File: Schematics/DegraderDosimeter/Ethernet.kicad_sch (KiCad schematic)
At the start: 38 parts, among them J1 KRJ-CB4.2GYZNL, U1 LAN8742A, U2 USBLC6-4SC6, U3 H1102NL, Y1 25.000MHz

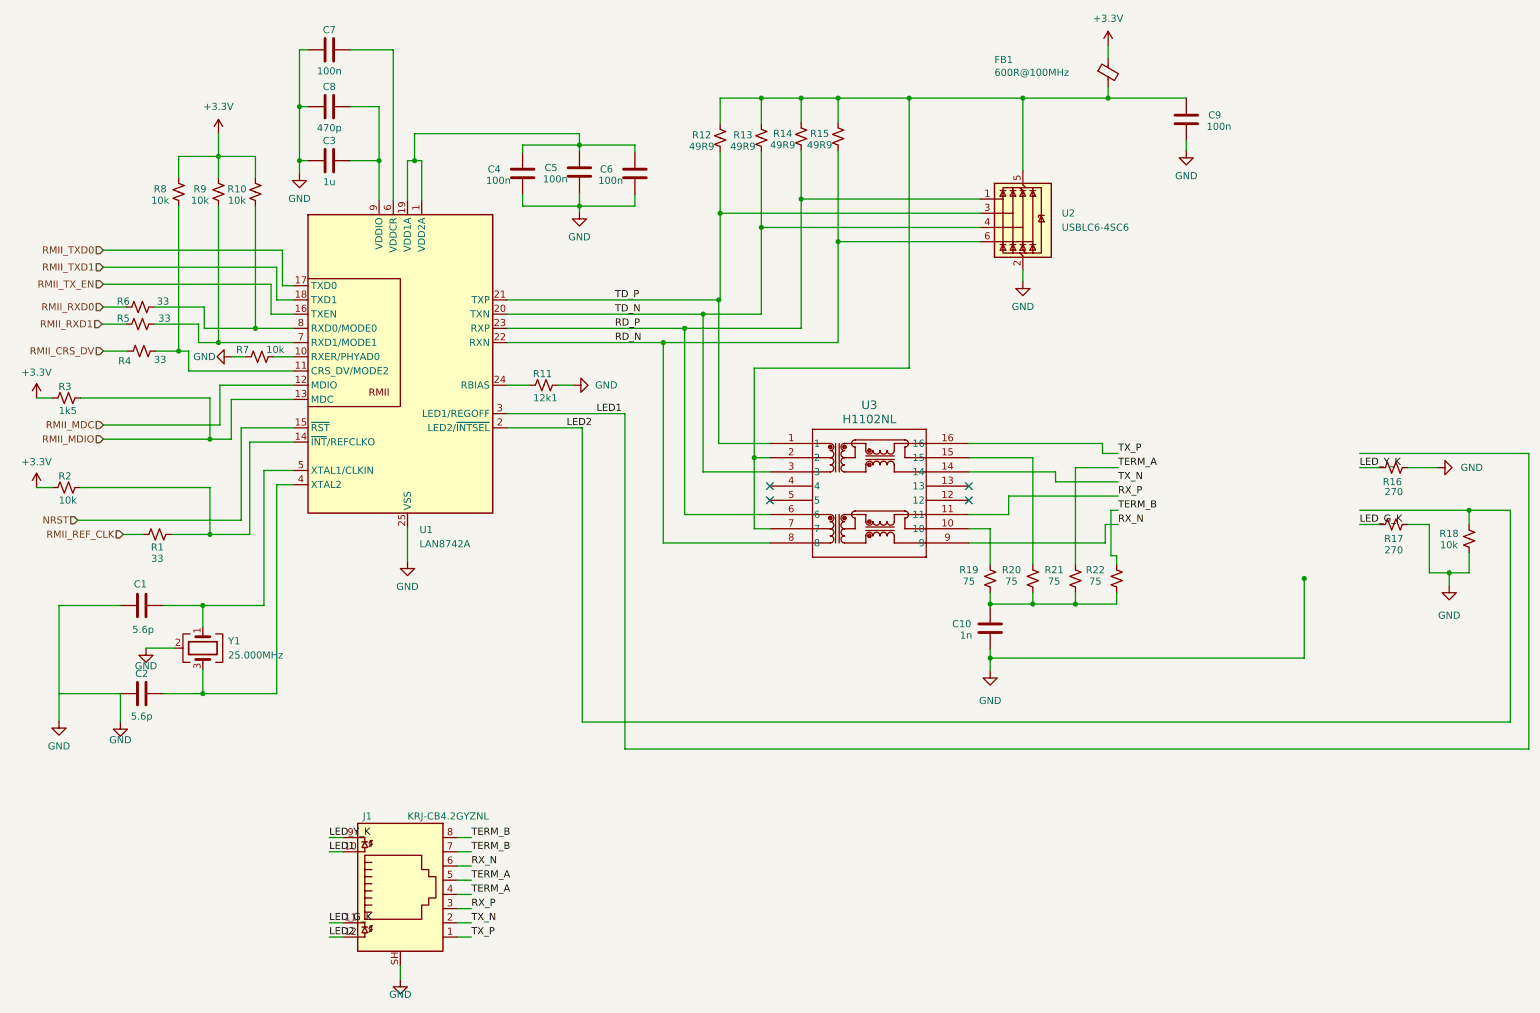
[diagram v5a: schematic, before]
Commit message: Use 1206 for every resistor in the project
The Ethernet sheet was the only one on 0402, set that way to match the
MB1364 BOM. The other four sheets already used
Resistor_SMD:R_1206_3216Metric_Pad1.30x1.75mm_HandSolder, so move the
20 Ethernet resistors to the same footprint. All 37 resistors in the
project now share one package, which suits hand assembly.

This deviates from the ST reference for the eight resistors on the
high-speed nets: R3-R6 (33R RMII series) and R12-R15 (49R9 centre-tap
terminations). 1206 has more parasitic inductance and larger pads than
the 0402 parts ST fits. 100BASE-TX is tolerant enough that this should
still work, but 0402 would be the better choice on those eight.

This commit also captures schematic edits made in KiCad outside this
session: a project-wide re-annotation and the removal of R21/R22, the
two 75R resistors that terminated the jack's unused pairs.

Co-Authored-By: Claude Opus 5 <noreply@anthropic.com>
Claude-Session: https://claude.ai/code/session_01Ej9hevrS5JU2uwVi6UHQUS
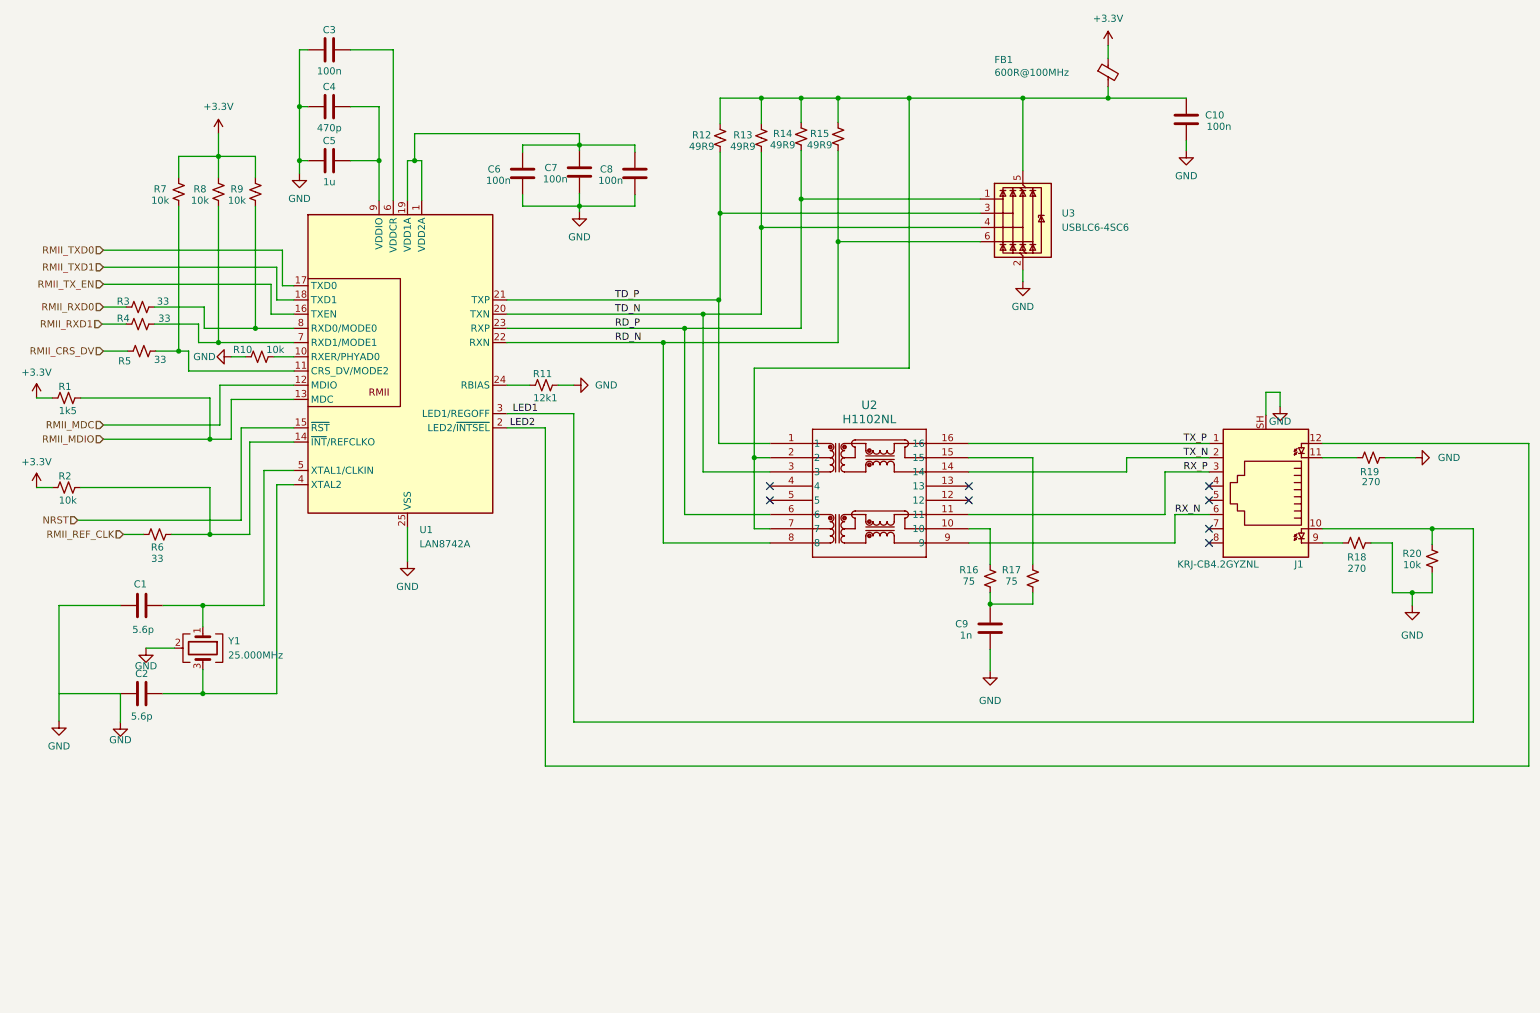
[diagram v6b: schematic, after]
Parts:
- removed R21, R22: 75, Resistor_SMD:R_0402_1005Metric, symbol Device:R_Small_US
- R1: renamed from R3; footprint Resistor_SMD:R_0402_1005Metric -> Resistor_SMD:R_1206_3216Metric_Pad1.30x1.75mm_HandSolder
- R10: renamed from R7; footprint Resistor_SMD:R_0402_1005Metric -> Resistor_SMD:R_1206_3216Metric_Pad1.30x1.75mm_HandSolder
- R11, R12, R13, R14, R15, R2: footprint Resistor_SMD:R_0402_1005Metric -> Resistor_SMD:R_1206_3216Metric_Pad1.30x1.75mm_HandSolder
- R16: renamed from R19; footprint Resistor_SMD:R_0402_1005Metric -> Resistor_SMD:R_1206_3216Metric_Pad1.30x1.75mm_HandSolder
- R17: renamed from R20; footprint Resistor_SMD:R_0402_1005Metric -> Resistor_SMD:R_1206_3216Metric_Pad1.30x1.75mm_HandSolder
- R18: renamed from R17; footprint Resistor_SMD:R_0402_1005Metric -> Resistor_SMD:R_1206_3216Metric_Pad1.30x1.75mm_HandSolder
- R19: renamed from R16; footprint Resistor_SMD:R_0402_1005Metric -> Resistor_SMD:R_1206_3216Metric_Pad1.30x1.75mm_HandSolder
- R20: renamed from R18; footprint Resistor_SMD:R_0402_1005Metric -> Resistor_SMD:R_1206_3216Metric_Pad1.30x1.75mm_HandSolder
- R3: renamed from R6; footprint Resistor_SMD:R_0402_1005Metric -> Resistor_SMD:R_1206_3216Metric_Pad1.30x1.75mm_HandSolder
- R4: renamed from R5; footprint Resistor_SMD:R_0402_1005Metric -> Resistor_SMD:R_1206_3216Metric_Pad1.30x1.75mm_HandSolder
- R5: renamed from R4; footprint Resistor_SMD:R_0402_1005Metric -> Resistor_SMD:R_1206_3216Metric_Pad1.30x1.75mm_HandSolder
- R6: renamed from R1; footprint Resistor_SMD:R_0402_1005Metric -> Resistor_SMD:R_1206_3216Metric_Pad1.30x1.75mm_HandSolder
- R7: renamed from R8; footprint Resistor_SMD:R_0402_1005Metric -> Resistor_SMD:R_1206_3216Metric_Pad1.30x1.75mm_HandSolder
- R8: renamed from R9; footprint Resistor_SMD:R_0402_1005Metric -> Resistor_SMD:R_1206_3216Metric_Pad1.30x1.75mm_HandSolder
- R9: renamed from R10; footprint Resistor_SMD:R_0402_1005Metric -> Resistor_SMD:R_1206_3216Metric_Pad1.30x1.75mm_HandSolder
- renumbered C9 to C10, C7 to C3, C8 to C4, C3 to C5, C4 to C6, C5 to C7, C6 to C8, C10 to C9, U3 to U2, U2 to U3
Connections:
- net LED1: now also R20.2
- net LED2: no longer R20.2
- net LED_G_K: no longer names the net of R18.2
- net LED_G_K: now also J1.9; no longer J1.11
- net LED_Y_K: no longer names the net of R19.1
- net LED_Y_K: now also J1.11; no longer J1.9
- net TERM_A: no longer names the net of J1.4
- net TERM_A: no longer J1.5
- net TERM_B: no longer names the net of J1.7
- net TERM_B: no longer J1.8
- no-connect marks 4 -> 8
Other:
- moved on the sheet: J1, R18, R19, R20

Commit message: Use 1206 for every capacitor in the project
Mirror of the resistor change: the nine remaining 0402 capacitors on the
Ethernet sheet move to Capacitor_SMD:C_1206_3216Metric, the footprint
the other 45 capacitors already use. All 54 capacitors and all 37
resistors in the project now sit on 1206.

C9 needed no change; the 1nF Bob Smith capacitor is 2kV rated
(CC1206KKX7RDBB102) and was already 1206.

Note for C1/C2, the 5.6pF crystal load capacitors: 1206 pads carry more
stray capacitance than 0402, which adds to the oscillator's effective
load and pulls X4 slightly low. The error is small enough to stay inside
the 50ppm that 100BASE-TX needs, but if the link proves marginal,
dropping C1/C2 to about 4.7pF compensates for the larger pads.

Co-Authored-By: Claude Opus 5 <noreply@anthropic.com>
Claude-Session: https://claude.ai/code/session_01Ej9hevrS5JU2uwVi6UHQUS
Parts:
- C1, C10, C2, C3, C4, C5, C6, C7, C8: footprint Capacitor_SMD:C_0402_1005Metric -> Capacitor_SMD:C_1206_3216Metric
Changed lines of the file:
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@@
 			)
 		)
-		(property "Footprint" "Capacitor_SMD:C_0402_1005Metric"
+		(property "Footprint" "Capacitor_SMD:C_1206_3216Metric"
 			(at 63.5 39.8272 0)
 			(hide yes)
@@
 			)
 		)
-		(property "Footprint" "Capacitor_SMD:C_0402_1005Metric"
+		(property "Footprint" "Capacitor_SMD:C_1206_3216Metric"
 			(at 63.5 20.0152 0)
 			(hide yes)
@@
 			)
 		)
-		(property "Footprint" "Capacitor_SMD:C_0402_1005Metric"
+		(property "Footprint" "Capacitor_SMD:C_1206_3216Metric"
 			(at 37.592 117.3988 0)
 			(hide yes)
@@
 			)
 		)
-		(property "Footprint" "Capacitor_SMD:C_0402_1005Metric"
+		(property "Footprint" "Capacitor_SMD:C_1206_3216Metric"
 			(at 37.592 133.1468 0)
 			(hide yes)
@@
 			)
 		)
-		(property "Footprint" "Capacitor_SMD:C_0402_1005Metric"
+		(property "Footprint" "Capacitor_SMD:C_1206_3216Metric"
 			(at 63.5 30.1752 0)
 			(hide yes)
@@
 			)
 		)
-		(property "Footprint" "Capacitor_SMD:C_0402_1005Metric"
+		(property "Footprint" "Capacitor_SMD:C_1206_3216Metric"
 			(at 102.8192 44.958 0)
 			(hide yes)
@@
 			)
 		)
-		(property "Footprint" "Capacitor_SMD:C_0402_1005Metric"
+		(property "Footprint" "Capacitor_SMD:C_1206_3216Metric"
 			(at 122.8852 44.958 0)
 			(hide yes)
@@
 			)
 		)
-		(property "Footprint" "Capacitor_SMD:C_0402_1005Metric"
+		(property "Footprint" "Capacitor_SMD:C_1206_3216Metric"
 			(at 112.9792 44.704 0)
 			(hide yes)
@@
 			)
 		)
-		(property "Footprint" "Capacitor_SMD:C_0402_1005Metric"
+		(property "Footprint" "Capacitor_SMD:C_1206_3216Metric"
 			(at 221.4372 35.306 0)
 			(hide yes)
